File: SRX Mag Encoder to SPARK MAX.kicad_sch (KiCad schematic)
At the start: 3 parts, among them J1 Conn_01x10_Pin, J2 Conn_01x10_Pin, J3 Conn_01x02_Pin

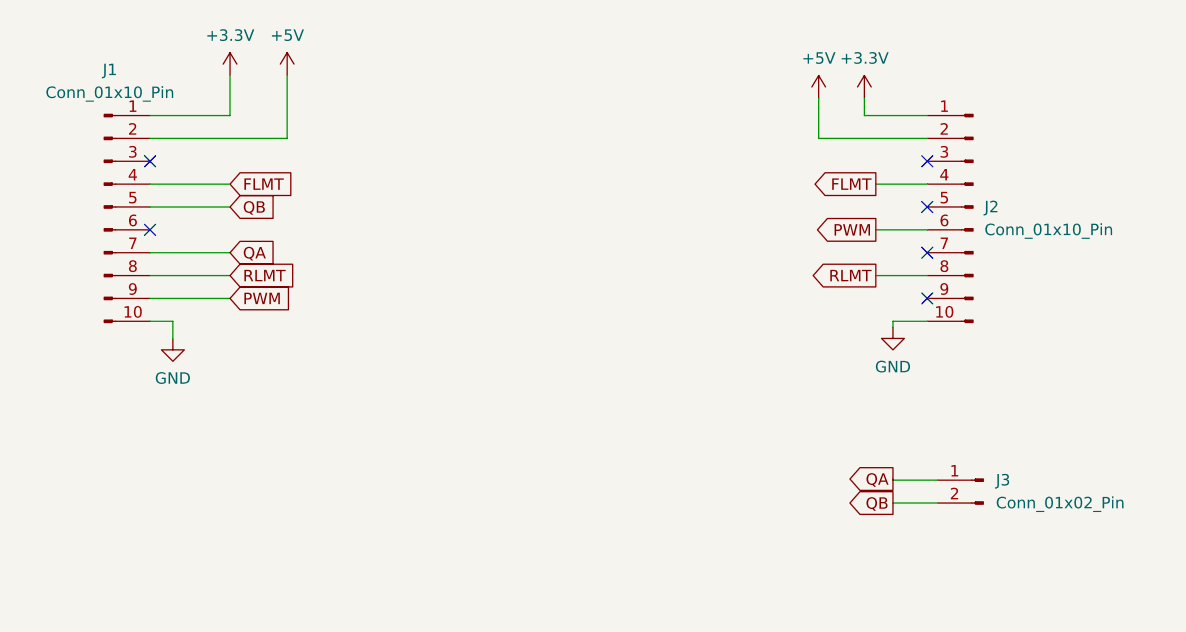
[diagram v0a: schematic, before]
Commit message: Routed power outputs to solder pads for roborio connection
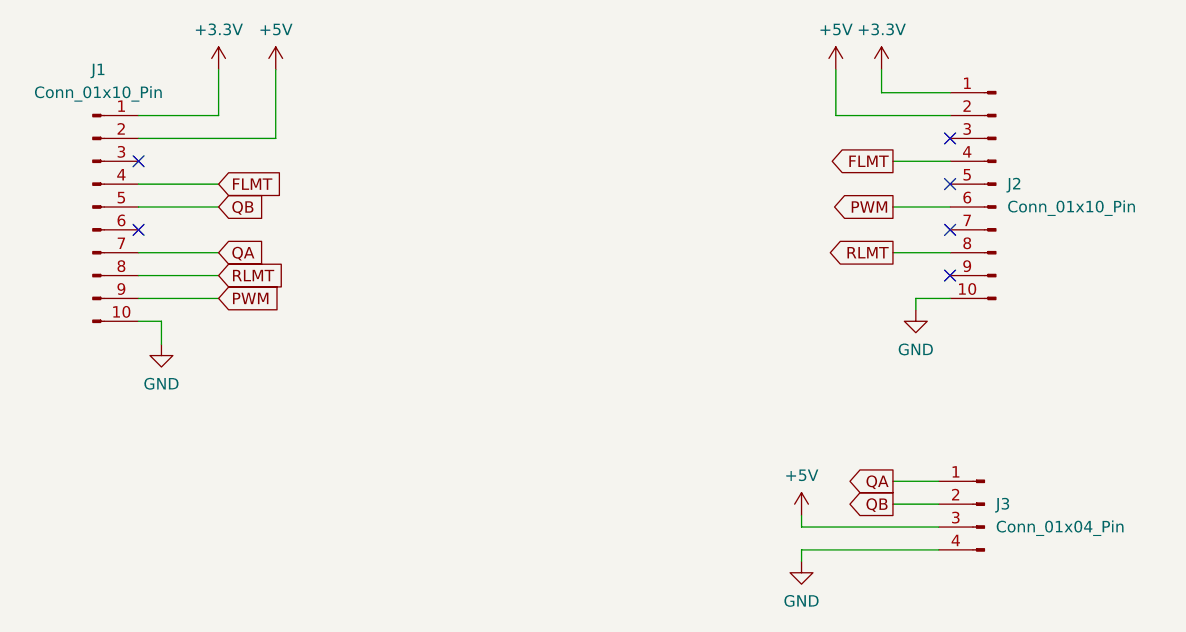
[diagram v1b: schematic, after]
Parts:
- removed J3: Conn_01x02_Pin, symbol Connector:Conn_01x02_Pin
- added J3: Conn_01x04_Pin, symbol Connector:Conn_01x04_Pin
- J1: footprint (none) -> footprints:3220-10-0300-00
- J2: footprint (none) -> footprints:CONN10_M50-3120545_HRW
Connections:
- net +5V: now also J3.3 (Pin_3)
- net GND: now also J3.4 (Pin_4)
- net QA: now also J3.1 (Pin_1)
- net QB: now also J3.2 (Pin_2)
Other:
- moved on the sheet: J1, J2
